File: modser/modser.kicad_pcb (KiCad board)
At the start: 2 copper layers, 3 parts, among them IC1 AS5600-ASOT, U1 DRV8313PWPR, U2 XIAO-RP2040-DIP

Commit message: Schematic draft complete!
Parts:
- added U3: AP63203WU-7, LIB_AP63203WU-7:AP63203WU7, F.Cu at (122.0, 79.3)
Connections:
- IC1 pad 1: unconnected-(IC1-VDD5V-Pad1) -> +3.3V
- IC1 pad 2: unconnected-(IC1-VDD3V3-Pad2) -> +3.3V
- IC1 pad 4: unconnected-(IC1-GND-Pad4) -> GND
- IC1 pad 6: unconnected-(IC1-SDA-Pad6) -> Net-(IC1-SDA)
- IC1 pad 7: unconnected-(IC1-SCL-Pad7) -> Net-(IC1-SCL)
- IC1 pad 8: unconnected-(IC1-DIR-Pad8) -> GND
- U1 pad 1: unconnected-(U1-CPL-Pad1) -> Net-(U1-CPL)
- U1 pad 10: unconnected-(U1-PGND3-Pad10) -> GND
- U1 pad 11: unconnected-(U1-VM__1-Pad11) -> VCC
- U1 pad 12: unconnected-(U1-COMPP-Pad12) -> GND
- U1 pad 13: unconnected-(U1-COMPN-Pad13) -> GND
- U1 pad 14: unconnected-(U1-GND-Pad14) -> GND
- U1 pad 15: unconnected-(U1-V3P3-Pad15) -> +3.3V
- U1 pad 18: unconnected-(U1-~{FAULT}-Pad18) -> Net-(U1-~{FAULT})
- U1 pad 19: unconnected-(U1-~{COMPO}-Pad19) -> GND
- U1 pad 2: unconnected-(U1-CPH-Pad2) -> Net-(U1-CPH)
- U1 pad 20: unconnected-(U1-GND__1-Pad20) -> GND
- U1 pad 22: unconnected-(U1-EN3-Pad22) -> Enable
- U1 pad 23: unconnected-(U1-IN3-Pad23) -> Net-(U1-IN3)
- U1 pad 24: unconnected-(U1-EN2-Pad24) -> Enable
- U1 pad 25: unconnected-(U1-IN2-Pad25) -> Net-(U1-IN2)
- U1 pad 26: unconnected-(U1-EN1-Pad26) -> Enable
- U1 pad 27: unconnected-(U1-IN1-Pad27) -> Net-(U1-IN1)
- U1 pad 28: unconnected-(U1-GND__2-Pad28) -> GND
- U1 pad 3: unconnected-(U1-VCP-Pad3) -> Net-(U1-VCP)
- U1 pad 4: unconnected-(U1-VM-Pad4) -> VCC
- U1 pad 5: unconnected-(U1-OUT1-Pad5) -> Net-(J1-Pin_1)
- U1 pad 6: unconnected-(U1-PGND1-Pad6) -> GND
- U1 pad 7: unconnected-(U1-PGND2-Pad7) -> GND
- U1 pad 8: unconnected-(U1-OUT2-Pad8) -> Net-(J1-Pin_2)
- U1 pad 9: unconnected-(U1-OUT3-Pad9) -> Net-(J1-Pin_3)
- U2 pad 1: unconnected-(U2-GPIO26/ADC0/A0-Pad1) -> Net-(U1-IN1)
- U2 pad 12: unconnected-(U2-3V3-Pad12) -> +3.3V
- U2 pad 13: unconnected-(U2-GND-Pad13) -> GND
- U2 pad 2: unconnected-(U2-GPIO27/ADC1/A1-Pad2) -> Net-(U1-IN2)
- U2 pad 3: unconnected-(U2-GPIO28/ADC2/A2-Pad3) -> Net-(U1-IN3)
- U2 pad 4: unconnected-(U2-GPIO29/ADC3/A3-Pad4) -> Enable
- U2 pad 5: unconnected-(U2-GPIO6/SDA-Pad5) -> Net-(IC1-SDA)
- U2 pad 6: unconnected-(U2-GPIO7/SCL-Pad6) -> Net-(IC1-SCL)

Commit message: Created general outline, speced passives
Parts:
- removed IC1: AS5600-ASOT, AS5600-ASOT:SOIC127P600X175-8N
- removed U1: DRV8313PWPR, DRV8313PWPR:SOP65P640X120-29N
- removed U2: XIAO-RP2040-DIP, Seeed_Studio_XIAO_Series:XIAO-RP2040-DIP
- removed U3: AP63203WU-7, LIB_AP63203WU-7:AP63203WU7
- added C1: 100 nF, Capacitor_SMD:C_0603_1608Metric_Pad1.08x0.95mm_HandSolder, F.Cu at (139.1, 84.0)
- added C10: 22 uF, Capacitor_SMD:C_1206_3216Metric, F.Cu at (138.5, 76.7)
- added C11: 22 uF, Capacitor_SMD:C_1206_3216Metric, F.Cu at (138.5, 80.0)
- added C3: 0.47 uF, Capacitor_SMD:C_0603_1608Metric_Pad1.08x0.95mm_HandSolder, F.Cu at (133.5, 72.9)
- added C4: 100 nF, Capacitor_SMD:C_0603_1608Metric_Pad1.08x0.95mm_HandSolder, F.Cu at (133.5, 75.4)
- added C5: 10 nF, Capacitor_SMD:C_0603_1608Metric_Pad1.08x0.95mm_HandSolder, F.Cu at (133.5, 77.9)
- added C6: 100 nF, Capacitor_SMD:C_0603_1608Metric_Pad1.08x0.95mm_HandSolder, F.Cu at (133.5, 80.4)
- added C7: 10 uF, Capacitor_SMD:C_1206_3216Metric, F.Cu at (138.5, 73.3)
- added C8: 100 nF, Capacitor_SMD:C_0603_1608Metric_Pad1.08x0.95mm_HandSolder, F.Cu at (133.5, 82.9)
- added C9: 100 pF, Capacitor_SMD:C_0603_1608Metric_Pad1.08x0.95mm_HandSolder, F.Cu at (133.5, 85.4)
- added J1: Conn_01x03_Socket, Connector_PinHeader_2.54mm:PinHeader_1x03_P2.54mm_Vertical, F.Cu at (113.5, 91.5)
- added J3: Conn_01x02_Socket, Connector_PinHeader_2.54mm:PinHeader_1x02_P2.54mm_Vertical, F.Cu at (156.0, 95.7)
- added R1: 10 kOhm, Resistor_SMD:R_0603_1608Metric_Pad0.98x0.95mm_HandSolder, F.Cu at (132.5, 96.4)
- added R2: 30.9 kOhm, Resistor_SMD:R_0603_1608Metric_Pad0.98x0.95mm_HandSolder, F.Cu at (132.5, 98.9)
- added R3: 62 kOhm, Resistor_SMD:R_0603_1608Metric_Pad0.98x0.95mm_HandSolder, F.Cu at (132.5, 101.4)
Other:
- board outline added: 25 x 25 mm

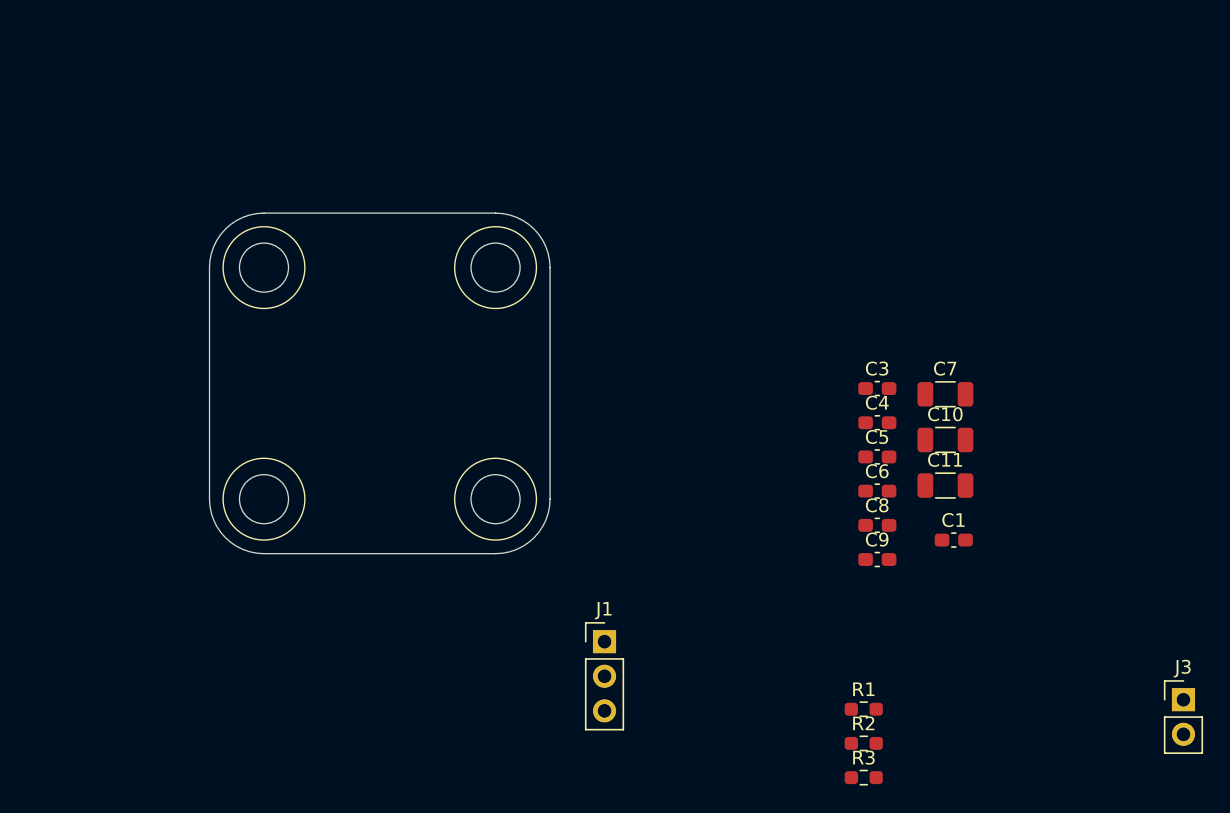
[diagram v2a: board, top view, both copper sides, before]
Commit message: Finished layout, working on getting all 3d models added
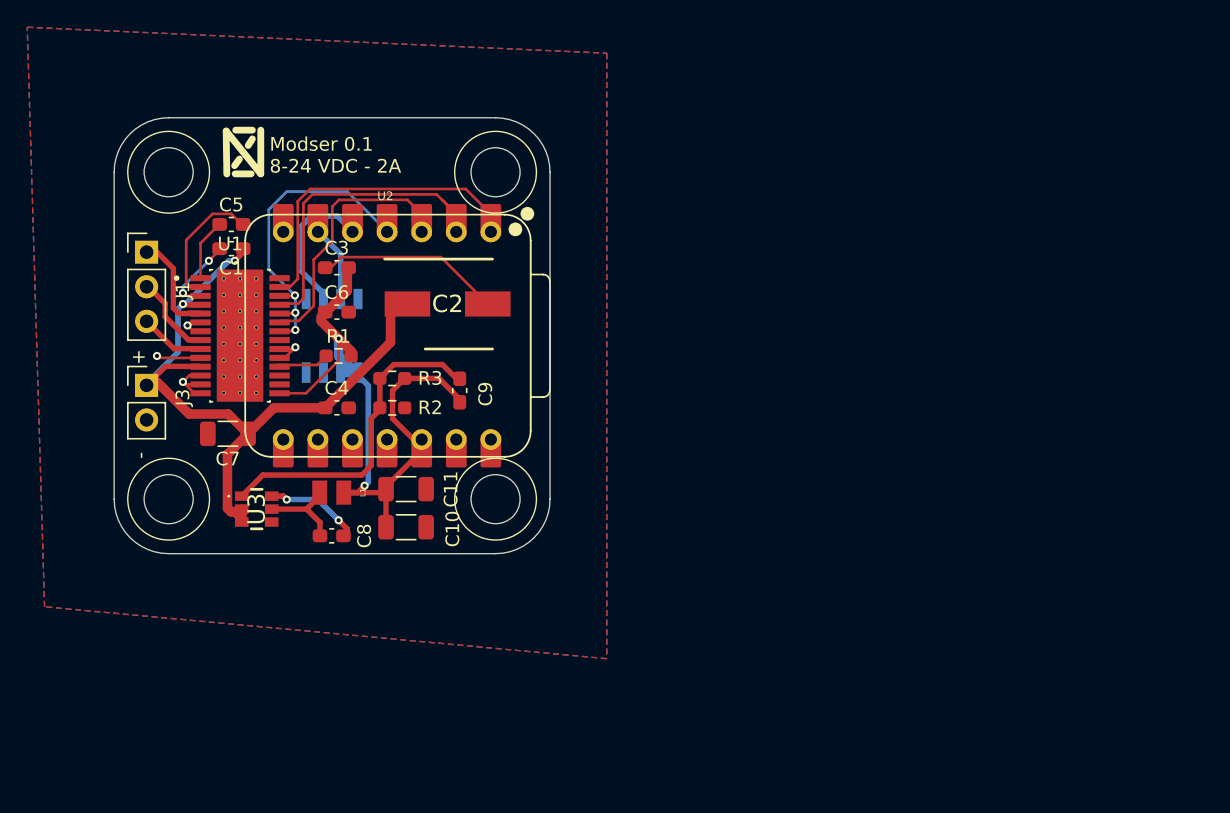
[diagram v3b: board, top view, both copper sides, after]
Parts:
- added C2: 100 uF Polarized, LIB_UCL1E101MCL1GS:CAPAE660X800N, F.Cu at (102.0, 66.7)
- added IC1: AS5600-ASOT, AS5600-ASOT:SOIC127P600X175-8N, B.Cu at (93.5, 69.0)
- added L1: 2.2 uH, LQM2MPN2R2NG0L:INDC2016X100N, F.Cu at (93.5, 80.5)
- added U1: DRV8313PWPR, DRV8313PWPR:SOP65P640X120-29N, F.Cu at (86.7, 69.0)
- added U2: XIAO-RP2040-DIP, Seeed_Studio_XIAO_Series:XIAO-RP2040-DIP, F.Cu at (97.5, 69.0)
- added U3: AP63203WU-7, LIB_AP63203WU-7:AP63203WU7, F.Cu at (88.0, 81.7)
- moved J3 79.5 mm to (79.9, 72.6)
- moved C1 57.2 mm to (86.1, 62.6), turned to 180 degrees
- moved C7 52.8 mm to (85.9, 76.2), turned to 180 degrees
- moved C5 50.4 mm to (86.1, 60.8)
- moved R1 46.5 mm to (94.0, 70.5)
- moved J1 44.1 mm to (79.9, 62.9)
- moved R3 44.0 mm to (97.9, 74.3)
- moved R2 43.8 mm to (97.9, 72.1), turned to 180 degrees
- moved C6 41.8 mm to (93.9, 67.3)
- moved C3 40.7 mm to (93.9, 64.0)
- moved C10 40.1 mm to (98.9, 83.1)
- moved C8 40.1 mm to (93.5, 83.7), turned to 180 degrees
- moved C4 39.7 mm to (93.9, 74.3)
- moved C11 39.6 mm to (98.9, 80.3)
- moved C9 33.1 mm to (102.9, 73.0), turned to 90 degrees
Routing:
- net VCC: track 0.00 -> 51.8 mm, vias 0 -> 2
- net +3.3V: track 0.00 -> 51.2 mm, vias 0 -> 2
- net GND: track 0.00 -> 26.0 mm, vias 0 -> 4
- net RegFB: track 0.00 -> 24.0 mm
- net Enable: track 0.00 -> 23.1 mm, vias 0 -> 3
- net Net-(U1-IN1): track 0.00 -> 22.1 mm
- net Net-(U1-IN2): track 0.00 -> 21.4 mm
- net Net-(U1-IN3): track 0.00 -> 17.5 mm
- net Net-(IC1-SDA): track 0.00 -> 10.9 mm
- net Net-(U1-CPH): track 0.00 -> 9.69 mm
- net Net-(J1-Pin_1): track 0.00 -> 7.63 mm
- net Net-(U3-BST): track 0.00 -> 7.18 mm, vias 0 -> 2
- net Net-(U3-SW): track 0.00 -> 6.46 mm
- net Net-(J1-Pin_2): track 0.00 -> 5.98 mm
- net Net-(U1-VCP): track 0.00 -> 5.44 mm, vias 0 -> 2
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- added copper zone on B.Cu, net GND
- added copper zone on F.Cu, net GND
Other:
- board size 25 x 25 mm -> 32 x 32 mm
- board text added: "+"
- board text added: "-"
- board text added: "Modser 0.1 8-24 VDC - 2A"
